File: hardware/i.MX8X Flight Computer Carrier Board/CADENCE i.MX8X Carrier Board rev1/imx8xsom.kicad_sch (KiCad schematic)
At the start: 6 parts

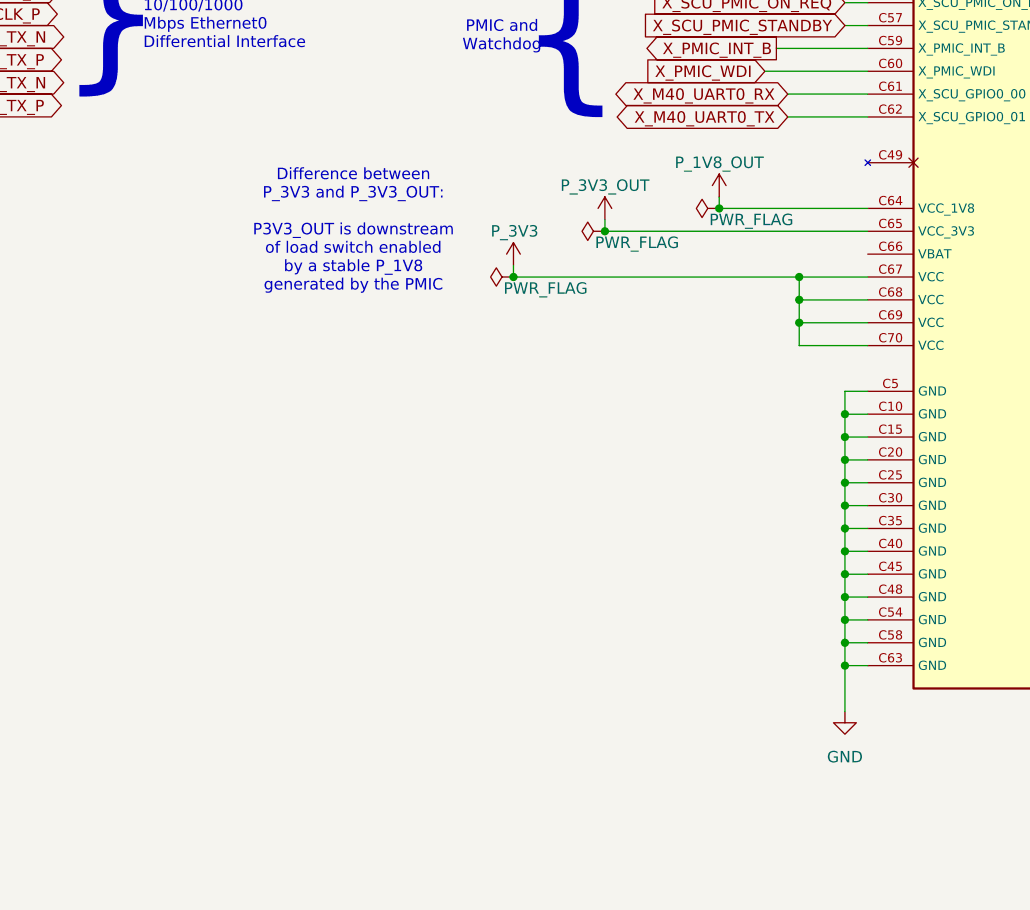
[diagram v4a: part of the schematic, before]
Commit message: just added coin batteries to gps and imx8x
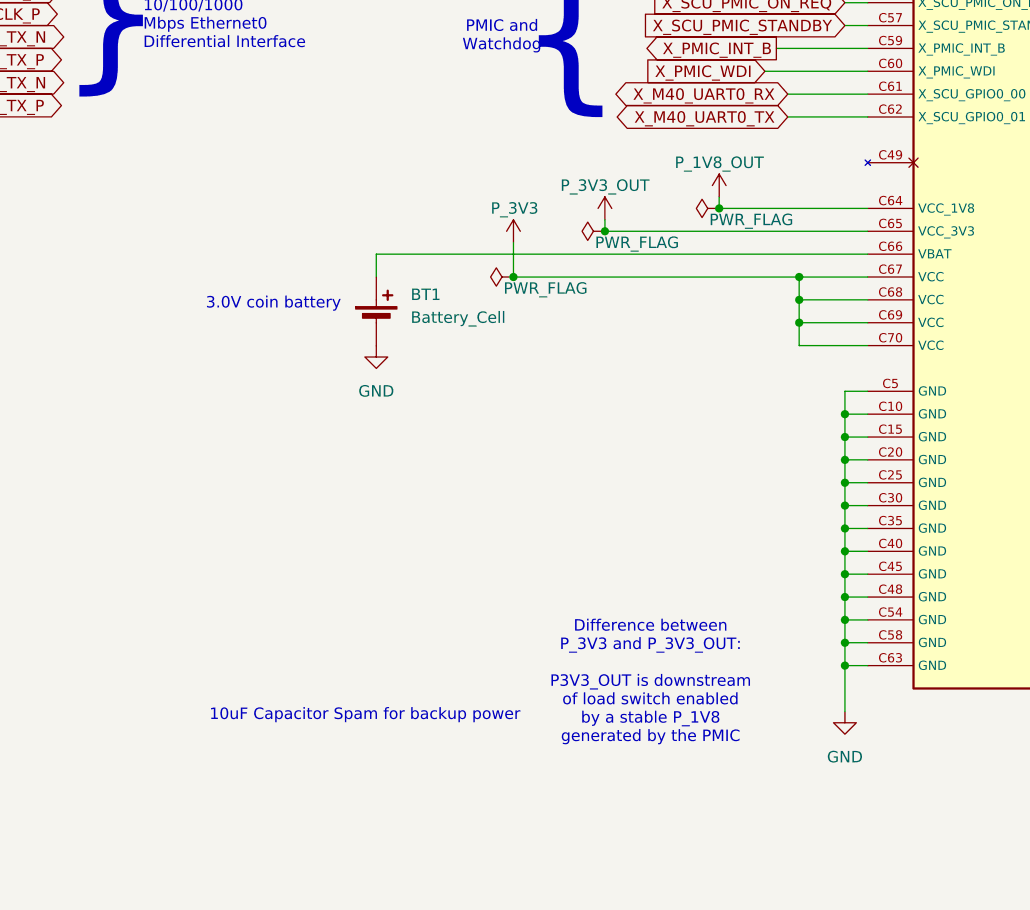
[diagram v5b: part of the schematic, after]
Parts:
- added BT1: Battery_Cell, symbol Device:Battery_Cell
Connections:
- net GND: now also BT1.2 (-)
- net at J?.C66 (VBAT): now also BT1.1 (+)
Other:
- note added: "10uF Capacitor Spam for backup power"
- note added: "3.0V coin battery"
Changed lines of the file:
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@@
 		)
 	)
+	(text "3.0V coin battery"
+		(exclude_from_sim no)
+		(at 251.46 215.138 0)
+		(effects
+			(font
+				(size 1.27 1.27)
+			)
+		)
+	)
 	(text "}"
 		(exclude_from_sim no)
@@
 	(text "Difference between \nP_3V3 and P_3V3_OUT:\n\nP3V3_OUT is downstream\nof load switch enabled\nby a stable P_1V8\ngenerated by the PMIC"
 		(exclude_from_sim no)
-		(at 260.35 207.01 0)
+		(at 293.37 257.175 0)
 		(effects
 			(font
@@
 		)
 	)
+	(text "10uF Capacitor Spam for backup power"
+		(exclude_from_sim no)
+		(at 261.62 260.858 0)
+		(effects
+			(font
+				(size 1.27 1.27)
+			)
+		)
+	)
 	(text "TO DO:\n- reorganize & fully implement board to board connections (SATNOGS should only need i2c now but double check; payload needs few i2c bus and rs422 if possible;adcs connection needs to be implemented)\n- double check octal spi nor flash memory implementation (very briefly skimmed datasheet)\n- add heater and antenna trigger connection/connector (need to talk with thermals & power about interface)\n- add more watchdog (for onboard power, satnogs)\n-assign watchdog input/output pins (pet pins, destination of outputs)\n-implement watchdog bite power cycling \n(load switch powering off processor briefly to force reset in case of radiation event)\n-add rs422 transceiver to payload connection/if possible\n-look into coin batteries for skytraq gnss and imx8x som (while also making sure safe in space)\n-connect RTC"
 		(exclude_from_sim no)
@@
 	(wire
 		(pts
+			(xy 262.89 209.55) (xy 262.89 212.09)
+		)
+		(stroke
+			(width 0)
+			(type default)
+		)
+	)
+	(wire
+		(pts
 			(xy 195.58 134.62) (xy 187.96 134.62)
 		)
@@
 	(wire
 		(pts
+			(xy 262.89 209.55) (xy 317.5 209.55)
+		)
+		(stroke
+			(width 0)
+			(type default)
+		)
+	)
+	(wire
+		(pts
 			(xy 109.22 205.74) (xy 127 205.74)
 		)
@@
 	(wire
 		(pts
-			(xy 278.13 210.82) (xy 278.13 212.09)
+			(xy 278.13 208.28) (xy 278.13 212.09)
 		)
 		(stroke
@@
 	)
 	(image
-		(at 260.35 220.98)
+		(at 293.37 271.145)
 		(scale 0.150355)
 		(data "iVBORw0KGgoAAAANSUhEUgAAAtsAAADSCAIAAAAUgpseAAAAA3NCSVQICAjb4U/gAAAACXBIWXMA"
@@
 	)
 	(symbol
+		(lib_id "power:GND")
+		(at 262.89 219.71 0)
+		(unit 1)
+		(exclude_from_sim no)
+		(in_bom yes)
+		(on_board yes)
+		(dnp no)
+		(fields_autoplaced yes)
+		(property "Reference" "#PWR016"
+			(at 262.89 226.06 0)
+			(effects
+				(font
+					(size 1.27 1.27)
+				)
+				(hide yes)
+			)
+		)
+		(property "Value" "GND"
+			(at 262.89 224.79 0)
+			(effects
+				(font
+					(size 1.27 1.27)
+				)
+			)
+		)
+		(property "Footprint" ""
+			(at 262.89 219.71 0)
+			(effects
+				(font
+					(size 1.27 1.27)
+				)
+				(hide yes)
+			)
+		)
+		(property "Datasheet" ""
+			(at 262.89 219.71 0)
+			(effects
+				(font
+					(size 1.27 1.27)
+				)
+				(hide yes)
+			)
+		)
+		(property "Description" "Power symbol creates a global label with name \"GND\" , ground"
+			(at 262.89 219.71 0)
+			(effects
+				(font
+					(size 1.27 1.27)
+				)
+				(hide yes)
+			)
+		)
+		(pin "1"
+		)
+		(instances
+			(project "CADENCE i.MX8X Carrier Board rev1"
+				(path "/de284495-d382-47cb-b528-76e440980d40/f5f49c98-aaea-4f03-a1b3-a277d1d06600"
+					(reference "#PWR016")
+					(unit 1)
+				)
+			)
+		)
+	)
+	(symbol
 		(lib_id "power:+3.3V")
 		(at 386.08 208.28 0)
@@
 	(symbol
 		(lib_id "power:+3.3V")
-		(at 278.13 210.82 0)
+		(at 278.13 208.28 0)
 		(unit 1)
 		(exclude_from_sim no)
@@
 		(dnp no)
 		(property "Reference" "#PWR040"
-			(at 278.13 214.63 0)
+			(at 278.13 212.09 0)
 			(effects
 				(font
@@
 		)
 		(property "Value" "P_3V3"
-			(at 275.59 207.01 0)
+			(at 275.59 204.47 0)
 			(effects
 				(font
@@
 		)
 		(property "Footprint" ""
-			(at 278.13 210.82 0)
+			(at 278.13 208.28 0)
 			(effects
 				(font
@@
 		)
 		(property "Datasheet" ""
-			(at 278.13 210.82 0)
+			(at 278.13 208.28 0)
 			(effects
 				(font
@@
 		)
 		(property "Description" "Power symbol creates a global label with name \"+3.3V\""
-			(at 278.13 210.82 0)
+			(at 278.13 208.28 0)
 			(effects
 				(font
@@
 				)
 			)
+		)
+	)
+	(symbol
+		(lib_id "Device:Battery_Cell")
+		(at 262.89 217.17 0)
+		(unit 1)
+		(exclude_from_sim no)
+		(in_bom yes)
+		(on_board yes)
+		(dnp no)
+		(fields_autoplaced yes)
+		(property "Reference" "BT1"
+			(at 266.7 214.0584 0)
+			(effects
+				(font
+					(size 1.27 1.27)
+				)
+				(justify left)
+			)
+		)
+		(property "Value" "Battery_Cell"
+			(at 266.7 216.5984 0)
+			(effects
+				(font
+					(size 1.27 1.27)
+				)
+				(justify left)
+			)
+		)
+		(property "Footprint" ""
+			(at 262.89 215.646 90)
+			(effects
+				(font
+					(size 1.27 1.27)
+				)
+				(hide yes)
+			)
+		)
+		(property "Datasheet" "~"
+			(at 262.89 215.646 90)
+			(effects
+				(font
+					(size 1.27 1.27)
+				)
+				(hide yes)
+			)
+		)
+		(property "Description" "Single-cell battery"
+			(at 262.89 217.17 0)
+			(effects
+				(font
+					(size 1.27 1.27)
+				)
+				(hide yes)
+			)
+		)
+		(pin "2"
+		)
+		(pin "1"
+		)
+		(instances
+			(project ""
+				(path "/de284495-d382-47cb-b528-76e440980d40/f5f49c98-aaea-4f03-a1b3-a277d1d06600"
+					(reference "BT1")
+					(unit 1)
+				)
+			)

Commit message: i2c onboard connection reorg, updated connection list,
also slight update to board connections.
prelim adcs board connection done, ebyte, satnogs, eps
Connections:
- net X_CSI_EN renamed X_CSI_EN_I2C3_SCL
- net X_CSI_RESET renamed X_CSI_RESET_I2C3_SDA
- net X_USB3_SS3_TC1 renamed X_USB3_SS3_TC1_I2C0_SCL
- net X_USB3_SS3_TC3 renamed X_USB3_SS3_TC3_I2C0_SDA
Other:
- note added: "I2C List(5 at 3.3V, 3 at 1.8V): I2C0: onboard RTC, IMU sensors, Temperature Sensors I2C1: Power Monitors I2C2: electrical power system management board I2c3: payload board i2c4: adcs connection likely (must further research cubespace adcs interface control document and connections. also adcs is still uncertain)"
- note added: "I2C3 (SATNOGS)"
- note added: "I2C4 (1.8V)"
- note added: "SPI List (2 devices per bus): SPI0:2x MRAM SPI1: SPI2:NAND Flash SPI3: SATNOGS and EByte"
- note added: "TO DO: - double check octal spi nor flash memory implementation - add heater and antenna trigger connection/connector (need to talk with thermals & power about interface) -assign watchdog input/output pins (pet pins, destination of outputs) -implement watchdog bite power cycling (load switch powering off processor briefly to force reset in case of radiation event) -add rs422 transceiver to payloa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"
- note added: "UART List(all at 3.3V except m40): UART0: GNSS UART1: Payload RS422 UART2: M40 UART: FTDI debug"
- note removed: "I2C List: I2C0: onboard RTC, IMU sensors, Temperature Sensors I2C1: Power Monitors I2C2: electrical power system management board I2c3 & I2C4: payload board i2c4: adcs connection likely (must further research cubespace adcs interface control document and connections. also adcs is still uncertain)"
- note removed: "TO DO: - reorganize & fully implement board to board connections (SATNOGS should only need i2c now but double check; payload needs few i2c bus and rs422 if possible;adcs connection needs to be implemented) - double check octal spi nor flash memory implementation (very briefly skimmed datasheet) - add heater and antenna trigger connection/connector (need to talk with thermals & power about interfa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"
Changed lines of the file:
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@@
 		)
 	)
-	(text "I2C List:\nI2C0: onboard RTC, IMU sensors, Temperature Sensors\nI2C1: Power Monitors\nI2C2: electrical power system management board\nI2c3 & I2C4: payload board\ni2c4: adcs connection likely (must further research cubespace adcs interface control document and connections. also adcs is still uncertain)\n"
+	(text "I2C List(5 at 3.3V, 3 at 1.8V):\nI2C0: onboard RTC, IMU sensors, Temperature Sensors\nI2C1: Power Monitors\nI2C2: electrical power system management board\nI2c3: payload board\ni2c4: adcs connection likely (must further research cubespace adcs interface control document and connections. also adcs is still uncertain)\n"
 		(exclude_from_sim no)
 		(at 323.088 368.046 0)
@@
 	(text "I2C1 (Onboard Power Monitors)"
 		(exclude_from_sim no)
-		(at 265.176 70.104 0)
+		(at 269.748 81.026 0)
+		(effects
+			(font
+				(size 1.27 1.27)
+			)
+		)
+	)
+	(text "I2C3 (SATNOGS)"
+		(exclude_from_sim no)
+		(at 443.992 99.822 0)
 		(effects
 			(font
@@
 	(text "}"
 		(exclude_from_sim no)
-		(at 233.172 71.628 0)
+		(at 231.902 71.882 0)
 		(effects
 			(font
@@
 	(text "I2C0 (Onboard Sensor Bus)"
 		(exclude_from_sim no)
-		(at 437.896 112.776 0)
+		(at 251.968 62.484 0)
 		(effects
 			(font
@@
 	(text "{"
 		(exclude_from_sim no)
-		(at 277.368 90.678 0)
+		(at 287.274 89.916 0)
 		(effects
 			(font
@@
 	(text "MIPI DSI0"
 		(exclude_from_sim no)
-		(at 268.224 92.202 0)
+		(at 278.638 91.948 0)
 		(effects
 			(font
@@
 	(text "USB 3.0"
 		(exclude_from_sim no)
-		(at 240.03 72.644 0)
+		(at 239.014 74.422 0)
 		(effects
 			(font
@@
 	(text "}"
 		(exclude_from_sim no)
-		(at 233.68 95.504 0)
+		(at 232.156 95.758 0)
 		(effects
 			(font
@@
 		)
 	)
+	(text "SPI List (2 devices per bus):\nSPI0:2x MRAM\nSPI1:\nSPI2:NAND Flash\nSPI3: SATNOGS and EByte"
+		(exclude_from_sim no)
+		(at 262.89 363.474 0)
+		(effects
+			(font
+				(size 5.08 5.08)
+				(thickness 1.016)
+				(bold yes)
+			)
+		)
+	)
 	(text "QSPI0"
 		(exclude_from_sim no)
@@
 		)
 	)
+	(text "UART List(all at 3.3V except m40):\nUART0: GNSS\nUART1: Payload RS422\nUART2:\nM40 UART: FTDI debug"
+		(exclude_from_sim no)
+		(at 128.524 363.728 0)
+		(effects
+			(font
+				(size 5.08 5.08)
+				(thickness 1.016)
+				(bold yes)
+			)
+		)
+	)
 	(text "10uF Capacitor Spam for backup power"
 		(exclude_from_sim no)
@@
 		)
 	)
-	(text "TO DO:\n- reorganize & fully implement board to board connections (SATNOGS should only need i2c now but double check; payload needs few i2c bus and rs422 if possible;adcs connection needs to be implemented)\n- double check octal spi nor flash memory implementation (very briefly skimmed datasheet)\n- add heater and antenna trigger connection/connector (need to talk with thermals & power about interface)\n- add more watchdog (for onboard power, satnogs)\n-assign watchdog input/output pins (pet pins, destination of outputs)\n-implement watchdog bite power cycling \n(load switch powering off processor briefly to force reset in case of radiation event)\n-add rs422 transceiver to payload connection/if possible\n-look into coin batteries for skytraq gnss and imx8x som (while also making sure safe in space)\n-connect RTC"
+	(text "TO DO:\n- double check octal spi nor flash memory implementation\n- add heater and antenna trigger connection/connector (need to talk with thermals & power about interface)\n-assign watchdog input/output pins (pet pins, destination of outputs)\n-implement watchdog bite power cycling \n(load switch powering off processor briefly to force reset in case of radiation event)\n-add rs422 transceiver to payload connection/if possible\n-connect RTC clkout? (32.768kHz default output, maybe to gpio?)\n-1PPS to GPIO?"
 		(exclude_from_sim no)
 		(at 324.358 427.736 0)
@@
 		)
 	)
+	(text "I2C4 (1.8V)"
+		(exclude_from_sim no)
+		(at 444.246 117.856 0)
+		(effects
+			(font
+				(size 1.27 1.27)
+			)
+		)
+	)
 	(junction
 		(at 386.08 212.09)
@@
 	(wire
 		(pts
+			(xy 187.96 66.04) (xy 237.49 66.04)
+		)
+		(stroke
+			(width 0)
+			(type default)
+		)
+	)
+	(wire
+		(pts
 			(xy 391.16 179.07) (xy 378.46 179.07)
 		)
@@
 	(wire
 		(pts
-			(xy 378.46 102.87) (xy 381 102.87)
+			(xy 378.46 102.87) (xy 426.72 102.87)
 		)
 		(stroke
@@
 	(wire
 		(pts
-			(xy 208.28 66.04) (xy 187.96 66.04)
-		)
-		(stroke
-			(width 0)
-			(type default)
-		)
-	)
-	(wire
-		(pts
 			(xy 187.96 236.22) (xy 190.5 236.22)
 		)
@@
 	(wire
 		(pts
-			(xy 378.46 105.41) (xy 381 105.41)
+			(xy 378.46 105.41) (xy 426.72 105.41)
 		)
 		(stroke
@@
 	(wire
 		(pts
-			(xy 276.86 74.93) (xy 317.5 74.93)
+			(xy 284.48 74.93) (xy 317.5 74.93)
 		)
 		(stroke
@@
 	(wire
 		(pts
-			(xy 208.28 71.12) (xy 187.96 71.12)
+			(xy 237.49 71.12) (xy 187.96 71.12)
 		)
 		(stroke
@@
 	(wire
 		(pts
-			(xy 276.86 77.47) (xy 317.5 77.47)
+			(xy 284.48 77.47) (xy 317.5 77.47)
 		)
 		(stroke
@@
 		)
 	)
+	(global_label "X_USB3_SS3_TC1_I2C0_SCL"
+		(shape bidirectional)
+		(at 261.62 36.83 0)
+		(effects
+			(font
+				(size 1.27 1.27)
+			)
+			(justify left)
+		)
+		(property "Intersheetrefs" "${INTERSHEET_REFS}"
+			(at 261.62 36.83 0)
+			(effects
+				(font
+					(size 1.27 1.27)
+				)
+				(hide yes)
+			)
+		)
+	)
 	(global_label "X_FLEXCAN1_TX"
 		(shape output)
@@
 		)
 	)
-	(global_label "X_USB3_SS3_TC1"
+	(global_label "X_USB3_SS3_TC1_I2C0_SCL"
 		(shape bidirectional)
-		(at 208.28 66.04 0)
+		(at 237.49 66.04 0)
 		(effects
 			(font
@@
 		)
 		(property "Intersheetrefs" "${INTERSHEET_REFS}"
-			(at 208.28 66.04 0)
+			(at 237.49 66.04 0)
 			(effects
 				(font
@@
 		)
 	)
+	(global_label "X_USB3_SS3_TC3_I2C0_SDA"
+		(shape bidirectional)
+		(at 261.62 39.37 0)
+		(effects
+			(font
+				(size 1.27 1.27)
+			)
+			(justify left)
+		)
+		(property "Intersheetrefs" "${INTERSHEET_REFS}"
+			(at 261.62 39.37 0)
+			(effects
+				(font
+					(size 1.27 1.27)
+				)
+				(hide yes)
+			)
+		)
+	)
 	(global_label "X_SAI0_TXC"
 		(shape output)
@@
 		)
 	)
-	(global_label "X_CSI_EN"
+	(global_label "X_CSI_EN_I2C3_SCL"
 		(shape bidirectional)
-		(at 381 102.87 0)
+		(at 426.72 102.87 0)
 		(effects
 			(font
@@
 		)
 		(property "Intersheetrefs" "${INTERSHEET_REFS}"
-			(at 381 102.87 0)
+			(at 426.72 102.87 0)
 			(effects
 				(font
@@
 		)
 	)
-	(global_label "X_USB3_SS3_TC3"
+	(global_label "X_USB3_SS3_TC3_I2C0_SDA"
 		(shape bidirectional)
-		(at 208.28 71.12 0)
+		(at 237.49 71.12 0)
 		(effects
 			(font
@@
 		)
 		(property "Intersheetrefs" "${INTERSHEET_REFS}"
-			(at 208.28 71.12 0)
+			(at 237.49 71.12 0)
 			(effects
 				(font
@@
 	(global_label "X_MIPI_DSI0_I2C0_SCL"
 		(shape bidirectional)
-		(at 276.86 77.47 180)
+		(at 284.48 77.47 180)
 		(effects
 			(font
@@
 		)
 		(property "Intersheetrefs" "${INTERSHEET_REFS}"
-			(at 276.86 77.47 0)
+			(at 284.48 77.47 0)
 			(effects
 				(font
@@
 	(global_label "X_MIPI_DSI0_I2C0_SDA"
 		(shape bidirectional)
-		(at 276.86 74.93 180)
+		(at 284.48 74.93 180)
 		(effects
 			(font
@@
 		)
 		(property "Intersheetrefs" "${INTERSHEET_REFS}"
-			(at 276.86 74.93 0)
+			(at 284.48 74.93 0)
 			(effects
 				(font
@@
 		)
 	)
-	(global_label "X_CSI_RESET"
+	(global_label "X_CSI_RESET_I2C3_SDA"
 		(shape bidirectional)
-		(at 381 105.41 0)
+		(at 426.72 105.41 0)
 		(effects
 			(font
@@
 		)
 		(property "Intersheetrefs" "${INTERSHEET_REFS}"
-			(at 381 105.41 0)
+			(at 426.72 105.41 0)
 			(effects
 				(font

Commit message: updated connections
-reset button
- fixed boot mode select
- i2c reorg/fixes
-added satnogs power monitor
-heater trigger connection (2gpio)
-more additions/fixes
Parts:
- removed BT1: Battery_Cell, symbol Device:Battery_Cell
- added C41, C42: 22uF, Capacitor_SMD:C_0603_1608Metric, symbol Device:C_Small
- added C43, C96: 4.7uF, Capacitor_SMD:C_0603_1608Metric, symbol Device:C_Small
- added C97: 100nF, Capacitor_SMD:C_0603_1608Metric, symbol Device:C_Small
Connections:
- net X_ADC_IN3 is gone; now on net X_M40_UART0_TX: J?.D62 (X_ADC_IN3)
- net GND: now also C41.2, C42.2, C43.2, C96.2, C97.2
- net P_3V3: now also C41.1, C42.1, C43.1, C96.1, C97.1
- net X_M40_UART0_TX: no longer J?.C62 (X_SCU_GPIO0_01)
- new net X_SCU_WDOG0_WDOG_OUT: J?.C62 (X_SCU_GPIO0_01)
- no-connect marks 0 -> 1
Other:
- note added: "TO DO: - double check octal spi nor flash memory implementation (max checked, but it seems part of qspi A is connected onboard flash, not fully sure on enabling ospi) - add heater and antenna trigger connection/connector(done, but need to talk with thermals & power about interface; current connector is preliminary) -implement watchdog bite power cycling (load switch powering off processor briefly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"
- note added: "X_MIPI_DSI0_GPIO0_00"
- note removed: "3.0V coin battery"
- note removed: "TO DO: - double check octal spi nor flash memory implementation - add heater and antenna trigger connection/connector (need to talk with thermals & power about interface) -assign watchdog input/output pins (pet pins, destination of outputs) -implement watchdog bite power cycling (load switch powering off processor briefly to force reset in case of radiation event) -add rs422 transceiver to payloa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"

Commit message: change RS422 power supply from 3.3 to 5 and a couple other changes
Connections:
- net X_SAI0_TXD renamed X_GPIO0_IO25
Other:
- moved on the sheet: C41, C42, C43, C96, C97, J?B
